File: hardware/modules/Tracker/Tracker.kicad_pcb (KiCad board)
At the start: 2 copper layers, 60 x 60 mm, 122 parts, among them J101 SMA, J102 SMA, J103 Battery, J104 Temp&Heater, J105 Ext Switch, J106 LiPo, Q101 Q_NMOS_GSD, Q102 Q_NMOS_GSD, Q103 Q_PMOS_GSD, Q104 Q_PMOS_GSD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

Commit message: 文字入れました
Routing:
- net /GPSActive/USB_D+: track 60.1 -> 48.1 mm
- net /ESP32/GPIO4/ADC1_CH3: vias 1 -> 0
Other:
- board text added: "2024 WASA Rockoon Tracker"
- board text added: "Backup"
- board text added: "CHARGE"
- board text added: "ERROR"
- board text added: "Ext Switch"
- board text added: "Heater"
- board text added: "Lipo"
- board text added: "RESET"
- board text added: "STAT"
- board text added: "USB P"
- board text added: "VDD"
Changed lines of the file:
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@@
 		(at 135.62 93.88 180)
 		(property "Reference" "U101"
-			(at 2.82 -1.89 180)
+			(at 31.48 1.34 180)
 			(layer "F.SilkS")
 			(effects
@@
 		(tags "LED")
 		(property "Reference" "LED105"
-			(at 0 -1.65 -90)
+			(at -0.3375 8.96 -90)
 			(layer "F.SilkS")
 			(effects
@@
 		(tags "LED")
 		(property "Reference" "LED101"
-			(at 0 -1.65 0)
+			(at 0.7975 -17.38 0)
 			(layer "F.SilkS")
 			(effects
@@
 		(tags "connector JST PH side entry")
 		(property "Reference" "J106"
-			(at 1 -2.9 0)
+			(at 0.08 -22.02 0)
 			(layer "F.SilkS")
 			(effects
@@
 		(tags "connector JST XH vertical")
 		(property "Reference" "J103"
-			(at 1.25 -3.55 0)
+			(at -0.59 -25.79 0)
 			(layer "F.SilkS")
 			(effects
@@
 		(tags "LED")
 		(property "Reference" "D108"
-			(at 0 -1.65 -90)
+			(at 1.45 -14.03 -90)
 			(layer "F.SilkS")
 			(effects
@@
 		(tags "LED")
 		(property "Reference" "D109"
-			(at 0 -1.65 90)
+			(at 11.3 27.84 90)
 			(layer "F.SilkS")
 			(effects
@@
 		(tags "LED")
 		(property "Reference" "LED102"
-			(at 0 -1.65 -90)
+			(at 26.59 -0.17 -90)
 			(layer "F.SilkS")
 			(effects
@@
 		(tags "LED")
 		(property "Reference" "LED103"
-			(at 0 -1.65 180)
+			(at 22.12 27.35 180)
 			(layer "F.SilkS")
 			(effects
@@
 		(tags "LED")
 		(property "Reference" "LED104"
-			(at 0 -1.65 180)
+			(at -17.28 1.49 180)
 			(layer "F.SilkS")
 			(effects
@@
 		(tags "connector JST PH side entry")
 		(property "Reference" "J105"
-			(at 1 -2.9 0)
+			(at 16.56 -2.93 0)
 			(layer "F.SilkS")
 			(effects
@@
 		(tags "capacitor")
 		(property "Reference" "C121"
-			(at 0 -1.16 90)
+			(at -8.26 -27.72 90)
 			(layer "F.SilkS")
 			(effects
@@
 			(at 4 0 -90)
 			(layer "B.Fab")
+			(hide yes)
 			(effects
 				(font
@@
 		)
 	)
+	(gr_text "STAT"
+		(at 134.18 110.21 90)
+		(layer "F.SilkS")
+		(effects
+			(font
+				(size 1 1)
+				(thickness 0.15)
+			)
+			(justify left bottom)
+		)
+	)
+	(gr_text "ERROR"
+		(at 136.32 111.55 90)
+		(layer "F.SilkS")
+		(effects
+			(font
+				(size 1 1)
+				(thickness 0.15)
+			)
+			(justify left bottom)
+		)
+	)
+	(gr_text "CHARGE"
+		(at 149.87 84.48 0)
+		(layer "F.SilkS")
+		(effects
+			(font
+				(size 1 1)
+				(thickness 0.15)
+			)
+			(justify left bottom)
+		)
+	)
+	(gr_text "Lipo"
+		(at 154.33 86.3 0)
+		(layer "F.SilkS")
+		(effects
+			(font
+				(size 1 1)
+				(thickness 0.15)
+			)
+			(justify left bottom)
+		)
+	)
+	(gr_text "RESET"
+		(at 126.46 82.77 0)
+		(layer "F.SilkS")
+		(effects
+			(font
+				(size 1 1)
+				(thickness 0.15)
+			)
+			(justify left bottom)
+		)
+	)
+	(gr_text "VDD"
+		(at 171.14 111.13 0)
+		(layer "F.SilkS")
+		(effects
+			(font
+				(size 1 1)
+				(thickness 0.15)
+			)
+			(justify left bottom)
+		)
+	)
+	(gr_text "USB P"
+		(at 136.16 85.64 0)
+		(layer "F.SilkS")
+		(effects
+			(font
+				(size 1 1)
+				(thickness 0.15)
+			)
+			(justify left bottom)
+		)
+	)
+	(gr_text "Heater"
+		(at 168.7 86.79 0)
+		(layer "F.SilkS")
+		(effects
+			(font
+				(size 1 1)
+				(thickness 0.15)
+			)
+			(justify left bottom)
+		)
+	)
+	(gr_text "Backup"
+		(at 144.86 91.69 0)
+		(layer "F.SilkS")
+		(effects
+			(font
+				(size 1 1)
+				(thickness 0.15)
+			)
+			(justify left bottom)
+		)
+	)
+	(gr_text "Heater"
+		(at 165.6 93.37 0)
+		(layer "F.SilkS")
+		(effects
+			(font
+				(size 1 1)
+				(thickness 0.15)
+			)
+			(justify left bottom)
+		)
+	)
+	(gr_text "Ext Switch"
+		(at 172.32 89.67 0)
+		(layer "F.SilkS")
+		(effects
+			(font
+				(size 1 1)
+				(thickness 0.15)
+			)
+			(justify left bottom)
+		)
+	)
+	(gr_text "2024 WASA Rockoon Tracker"
+		(at 123.16 119.14 0)
+		(layer "F.SilkS")
+		(effects
+			(font
+				(size 1.5 1.5)
+				(thickness 0.3)
+				(bold yes)
+			)
+			(justify left bottom)
+		)
+	)
 	(segment
 		(start 133.68 87.69)
@@
 	)
 	(segment
-		(start 154.885786 83.44)
-		(end 163.365787 91.920001)
-		(width 0.8)
-		(layer "B.Cu")
-		(net 9)
-	)
-	(segment
 		(start 173.80783 109.638344)
 		(end 175.525787 111.356301)
@@
 		(net 59)
 	)
-	(via
-		(at 136.43 86.542182)
-		(size 0.5)
-		(drill 0.3)
-		(layers "F.Cu" "B.Cu")
-		(net 59)
-	)

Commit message: 抵抗等変更しました
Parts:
- R116, R136: value 470k -> 47k
- R117: value 100k -> 10k
- R132: value 470k -> 330k
- R135: value 150k -> 15k
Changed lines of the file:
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@@
 			)
 		)
-		(property "Value" "470k"
+		(property "Value" "47k"
 			(at 0 1.17 0)
 			(layer "F.Fab")
@@
 			)
 		)
-		(property "LCSC" "C25790"
+		(property "LCSC" "C25792"
 			(at 0 0 0)
 			(unlocked yes)
@@
 			)
 		)
-		(property "Value" "150k"
+		(property "Value" "15k"
 			(at 0 1.17 180)
 			(layer "F.Fab")
@@
 			)
 		)
-		(property "LCSC" " C25755"
+		(property "LCSC" " C25756"
 			(at 0 0 180)
 			(unlocked yes)
@@
 			)
 		)
-		(property "Value" "470k"
+		(property "Value" "47k"
 			(at 0 1.17 90)
 			(layer "F.Fab")
@@
 			)
 		)
-		(property "LCSC" "C25790"
+		(property "LCSC" "C25792"
 			(at 0 0 -90)
 			(unlocked yes)
@@
 			)
 		)
-		(property "Value" "100k"
+		(property "Value" "10k"
 			(at 0 1.17 90)
 			(layer "F.Fab")
@@
 			)
 		)
-		(property "LCSC" "C25741"
+		(property "LCSC" "C25744"
 			(at 0 0 -90)
 			(unlocked yes)
@@
 			)
 		)
-		(property "LCSC" "C25139"
+		(property "LCSC" "C25077"
 			(at 0 0 -90)
 			(unlocked yes)
@@
 			)
 		)
-		(property "Value" "470k"
+		(property "Value" "330k"
 			(at 0 1.17 0)
 			(layer "F.Fab")
@@
 			)
 		)
-		(property "LCSC" "C25790"
+		(property "LCSC" "C23137"
 			(at 0 0 0)
 			(unlocked yes)

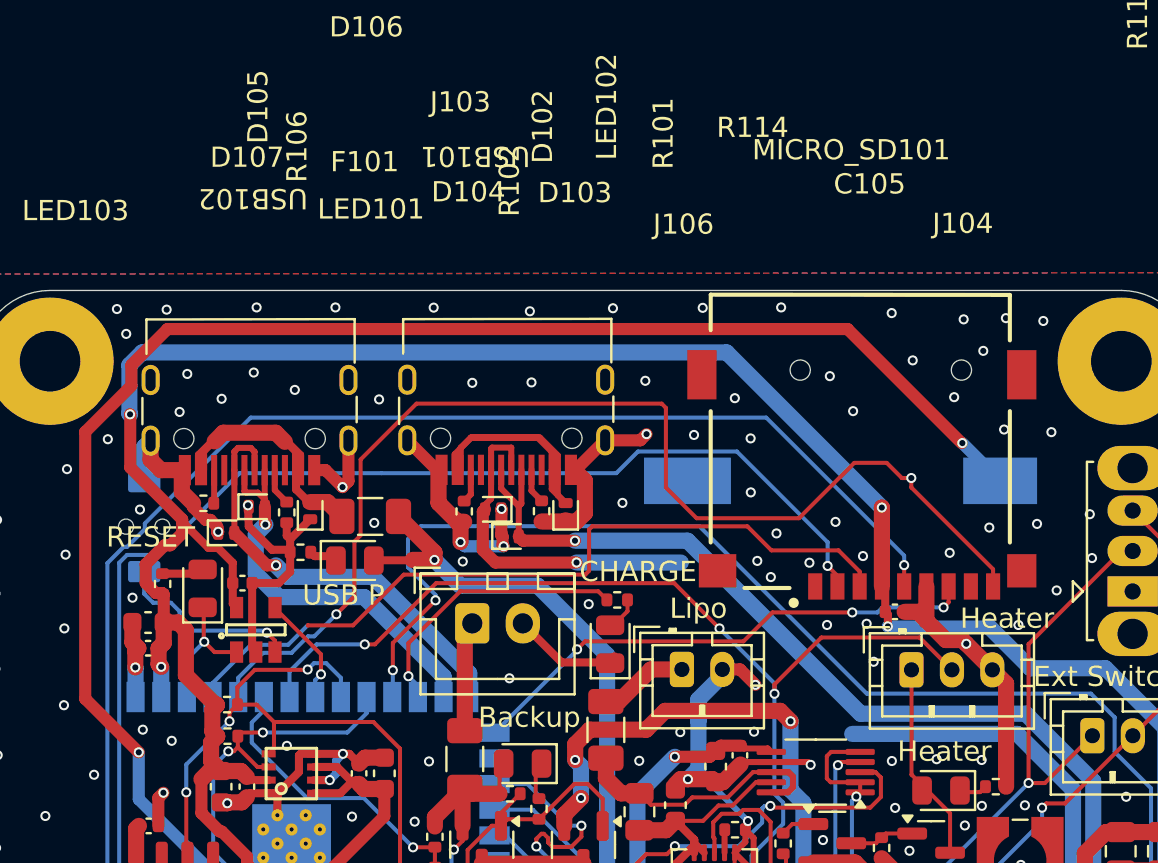
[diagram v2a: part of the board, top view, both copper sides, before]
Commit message: c105のフットプリント変更に伴う修正
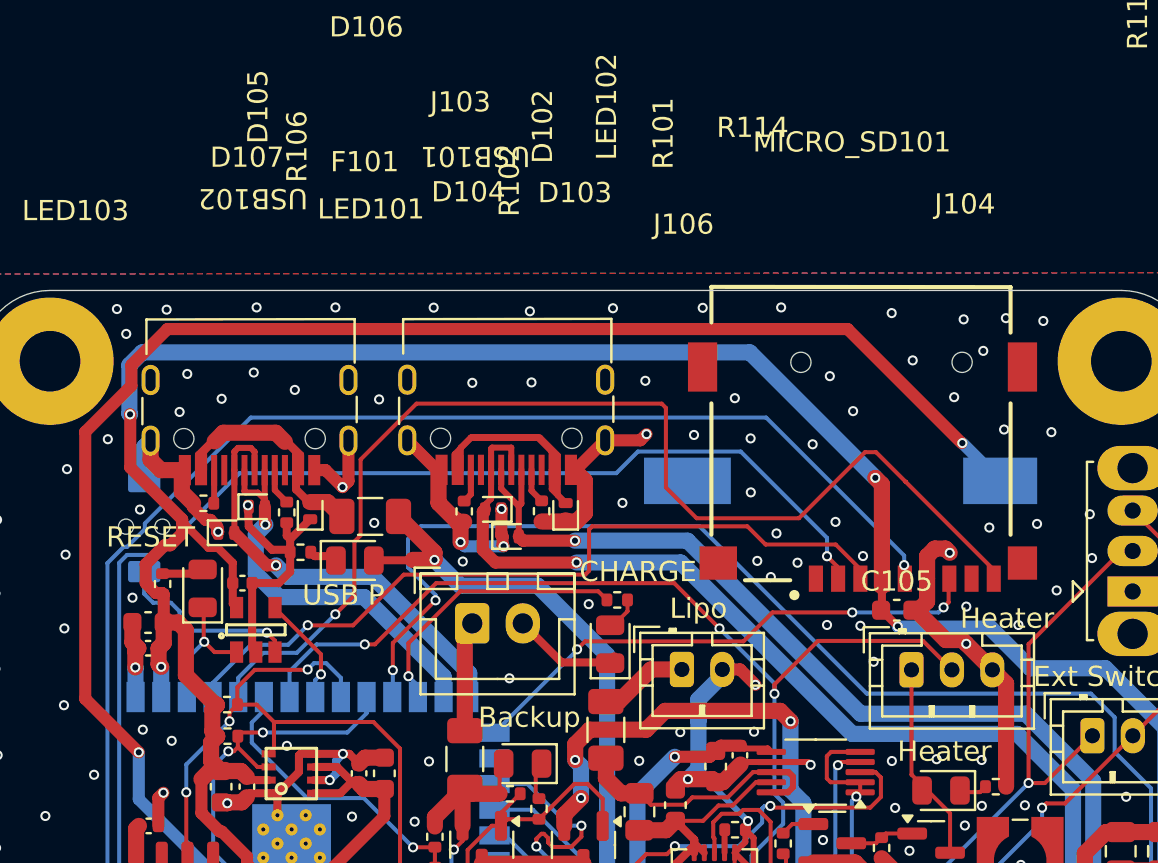
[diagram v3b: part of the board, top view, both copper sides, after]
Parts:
- C105: footprint Capacitor_SMD:C_0402_1005Metric -> Capacitor_SMD:C_0603_1608Metric
- moved MICRO_SD101 0.39 mm to (163.8, 77.1)
- moved C105 0.12 mm to (165.6, 85.8)
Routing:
- net /GPSActive/USB_D+: track 48.1 -> 60.1 mm
- net GND: track 223.5 -> 225.4 mm, vias 235 -> 237
- net /ESP32/GPIO5/ADC1_CH4: track 56.8 -> 56.9 mm, vias 2 -> 1
- net /ESP32/GPIO4/ADC1_CH3: track 38.8 -> 38.9 mm, vias 0 -> 1

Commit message: 微調整
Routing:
- net GND: track 225.4 -> 225.6 mm, vias 237 -> 244

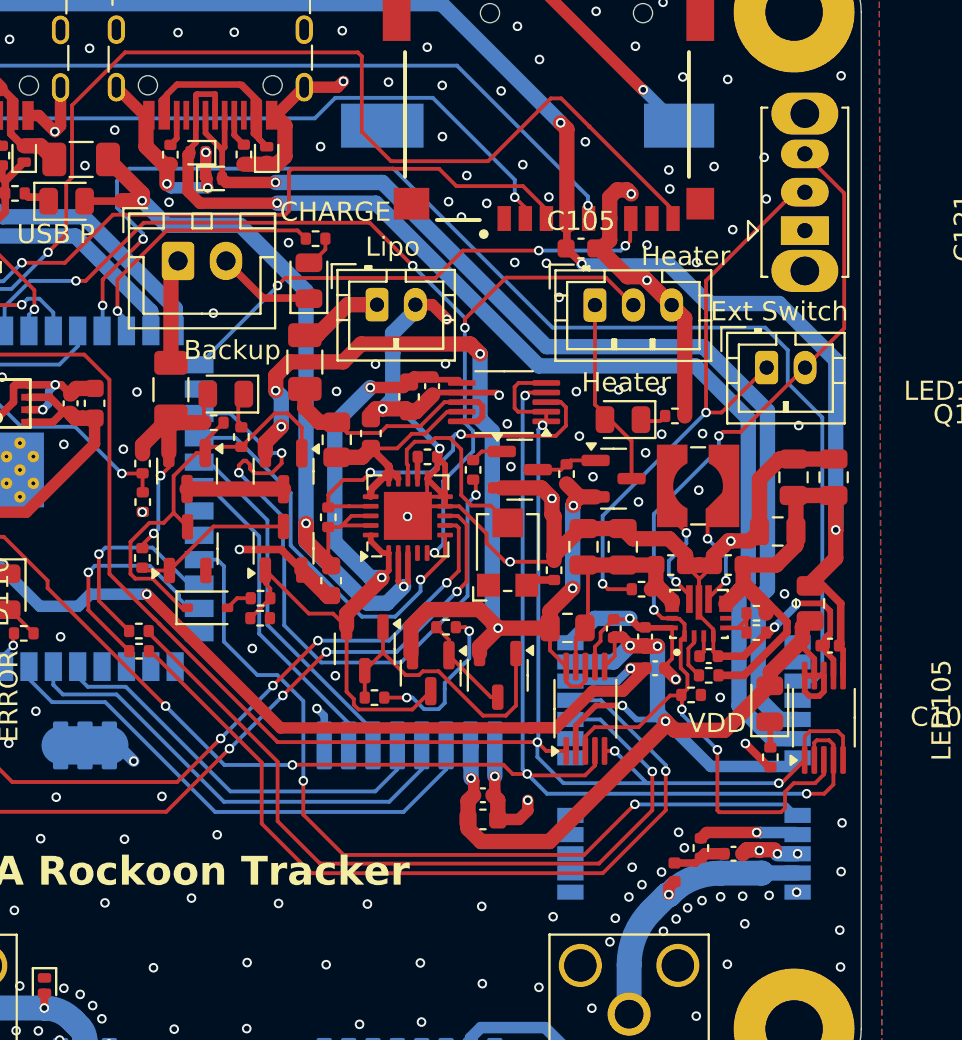
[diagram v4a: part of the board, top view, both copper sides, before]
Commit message: GPSのfootprint差し替え，lipo側INA(0x4F)のVSをVDDにつないだ.
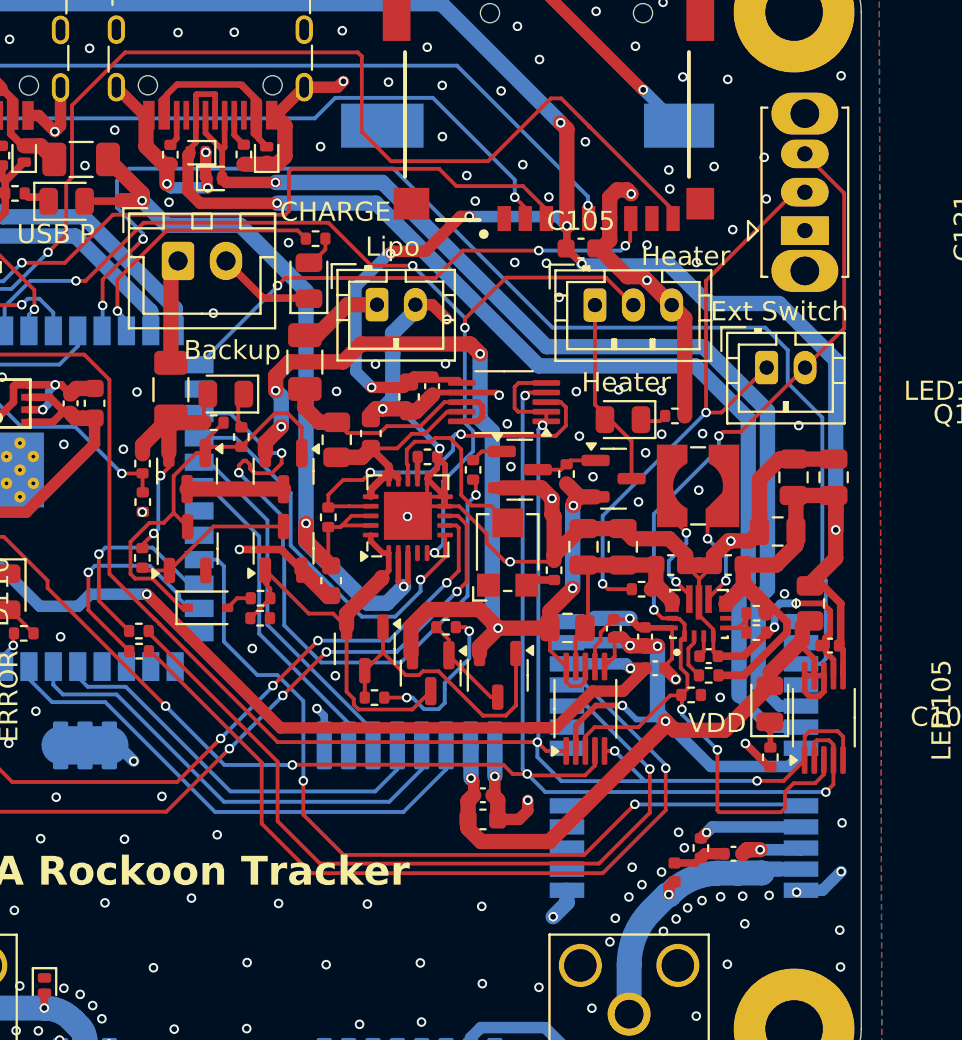
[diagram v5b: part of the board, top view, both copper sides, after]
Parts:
- U104: footprint WOBClibrary:SMT_9N-00B_UBL -> WOBClibrary:ATGM332D-5N31
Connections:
- C117 pad 1: Net-(Q102-G) -> VDD
- C121 pad 1: Net-(Q102-G) -> VDD
- U109 pad 6: Net-(Q102-G) -> VDD
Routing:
- net VDD: track 225.3 -> 249.1 mm, vias 10 -> 14
- net Net-(Q102-G): track 40.7 -> 23.5 mm, vias 2 -> 0
- net GND: track 225.6 -> 230.2 mm, vias 244 -> 240
- net unconnected-(U104-EXTINT-Pad4): track 0.00 -> 0.89 mm
- net /ESP32/GPIO21: track 44.7 -> 43.9 mm
- net /ESP32/GPIO18: track 67.5 -> 66.7 mm
- net /GPSActive/USB_D-: track 56.6 -> 56.1 mm
- net Net-(U104-RXD_/_SPI_MOSI): track 43.7 -> 44.2 mm

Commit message: usb type-Cのコネクタのプルダウン抵抗を22kΩから5.1kΩ(0402(basic))に変更
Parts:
- R101, R102, R106, R107: value 22k -> 5.1k
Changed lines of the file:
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@@
 			)
 		)
-		(property "Value" "22k"
+		(property "Value" "5.1k"
 			(at 0 1.17 90)
 			(layer "F.Fab")
@@
 			)
 		)
-		(property "Value" "22k"
+		(property "Value" "5.1k"
 			(at 0 1.17 90)
 			(layer "F.Fab")
@@
 			)
 		)
-		(property "Value" "22k"
+		(property "Value" "5.1k"
 			(at 0 1.17 180)
 			(layer "F.Fab")
@@
 			)
 		)
-		(property "Value" "22k"
+		(property "Value" "5.1k"
 			(at 0 1.17 90)
 			(layer "F.Fab")

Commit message: Igniteコンポーネントの作成とTrackerモジュールの修正
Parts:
- added R139: 10k, Resistor_SMD:R_0402_1005Metric, F.Cu at (138.9, 88.9)
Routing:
- net GND: track 230.2 -> 235.9 mm
- net /ESP32/GPIO9/ADC1_CH8: track 36.1 -> 37.1 mm
- net /ESP32/GPIO7/ADC1_CH6: track 53.5 -> 54.4 mm
